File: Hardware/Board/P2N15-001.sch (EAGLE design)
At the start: 36 parts, among them IC1 4053N, IC2 LTC485N, IC3 74LS07N, IC4 LTC485N, X1 HIROSE-DX10LM1-14SE, X2 SUNHAYATO-USB-CK37

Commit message: Redesigned N15 board.
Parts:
- removed IC3: 74LS07N, 74xx-us:74LS07N
- removed IC4: LTC485N, linear-technology:LTC485N
- removed JP3: (no value), pinhead:PINHD-2X3
- removed JP4: (no value), adafruit:PINHD-1X6
- removed LED1, LED2: (no value), led:LED3MM
- removed R10, R11, R12, R7, R8, R9: 220, resistor:R-US_0204/5
- removed R13, R6: 120, resistor:R-US_0204/5
- added S2: TL32PO, switch:TL32PO
- added SV2: (no value), con-ml:ML10L
- IC1: value 4053N -> TLC5941NT; device 40xx:4053N -> adafruit:TLC5941NT
- R3: value 330 -> 4.7k
- R4: value 330 -> 120
- SV1: device con-ml:ML10L -> con-ml:ML20L
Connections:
- removed net ANLG0: JP2.8, MC1.A0, X1.-8
- removed net ANLG1: JP2.9, MC1.A1, X1.-9
- removed net ANLG2: JP2.10, MC1.A2, X1.-10
- removed net ANLG3: JP2.11, MC1.A3, X1.-11
- removed net ANLG4: IC1A.X1, MC1.A4
- removed net ANLG5: IC1A.Y1, MC1.A5
- removed net MISO: JP3.4, MC1.MISO
- removed net RXRETURN: R5.2, SV1.3
- removed net RXSEND: R10.2, SV1.1
- removed net SCL: IC1A.Y0, MC1.3
- removed net SDA: IC1A.X0, MC1.2
- removed net SEL: IC1A.A, IC1A.B, MC1.7
- removed net TX: IC3A.I, IC3B.I, IC4.DI, MC1.TX
- removed net TX+: CN1.1, IC4.A, R13.2
- removed net TX-: CN1.2, IC4.B, R13.1
- removed net TX2RETURN: R11.2, SV1.5
- removed net TX2SEND: R9.2, SV1.4
- removed net TXRETURN: R12.2, SV1.8
- removed net TXSEND: R8.2, SV1.6
- removed net XMIDIRX: IC1A.Z1, IC2.RO
- new net N$10: IC1.OUT3, JP2.10, SV1.6, X1.-10
- new net N$11: IC1.OUT4, JP2.11, SV1.7, X1.-11
- new net N$12: IC1.OUT10, SV1.14
- new net N$13: IC1.OUT11, SV1.13
- new net N$14: IC1.OUT12, SV1.16
- new net N$16: IC1.OUT13, SV1.15
- new net N$7: IC1.OUT1, JP2.8, SV1.4, X1.-8
- new net N$9: IC1.OUT2, JP2.9, SV1.5, X1.-9
- net GND: now also IC1.GND, IC1.MODE, R3.1, SV1.1; no longer IC1A.INH, IC3D.I, IC3E.I, IC3F.I, IC4.GND, JP2.14, JP4.5, R3.2, R4.2, SV1.2, SV1.7, X1.-14
- net GPIO0: now also IC1.GSCLK; no longer JP3.1, LED1.A
- net GPIO1: now also IC1.BLANK; no longer JP3.2, LED2.A
- net GPIO2: now also IC1.XLAT; no longer JP3.3
- net MIDIRX: now also S2.O; no longer IC1A.Z0, IC3C.I
- net MOSI: now also IC1.SIN; no longer JP3.5
- net N$15: now also R5.1; no longer R7.1
- net N$17: now also IC1.OUT14, SV1.18; no longer LED1.C, R3.1
- net N$18: now also IC1.OUT15, SV1.17; no longer LED2.C, R4.1
- net N$2: now also IC2.RO, S2.S; no longer IC3A.O, R11.1
- net N$28: now also IC1.OUT5, SV1.8; no longer IC1A.X
- net N$29: now also IC1.OUT6, SV1.9; no longer IC1A.Y
- net N$3: now also IC1.OUT0, JP2.7, SV1.3, X1.-7; no longer IC3C.O, R5.1
- net N$4: now also IC1.IREF, R3.2; no longer IC3B.O, R12.1
- net N$5: now also IC1.OUT7, JP2.14, SV1.10, X1.-14; no longer JP4.2, MC1.9
- net N$6: now also IC1.OUT8, SV1.12; no longer JP4.3, MC1.10
- net N$8: now also IC1.OUT9, SV1.11; no longer IC1A.C, MC1.4
- net PD: no longer JP4.1
- net RX: now also S2.P
- net RX+: now also R4.2; no longer R6.2
- net RX-: now also R4.1; no longer R6.1
- net RXA: now also R5.2, SV2.9; no longer R7.2, SV1.9
- net RXK: now also SV2.10; no longer SV1.10
- net SCLK: now also IC1.SCLK; no longer JP3.6
- net VCC: now also IC1.TEST, IC1.VCC; no longer IC4.!RE, IC4.DE, IC4.VCC, JP2.7, R10.1, R8.1, R9.1, X1.-7
- net VDD: now also SV1.2
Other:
- note removed: "1: GPIO 0; 2: GPIO 1; 2: GPIO 3; 4: MISO; 5: MOSI; 6: SCLCK"
- note removed: "1: TXA; 2: TXK 3: RXA; 4: RXK"
- moved on the sheet: R3, R4, R5, X2

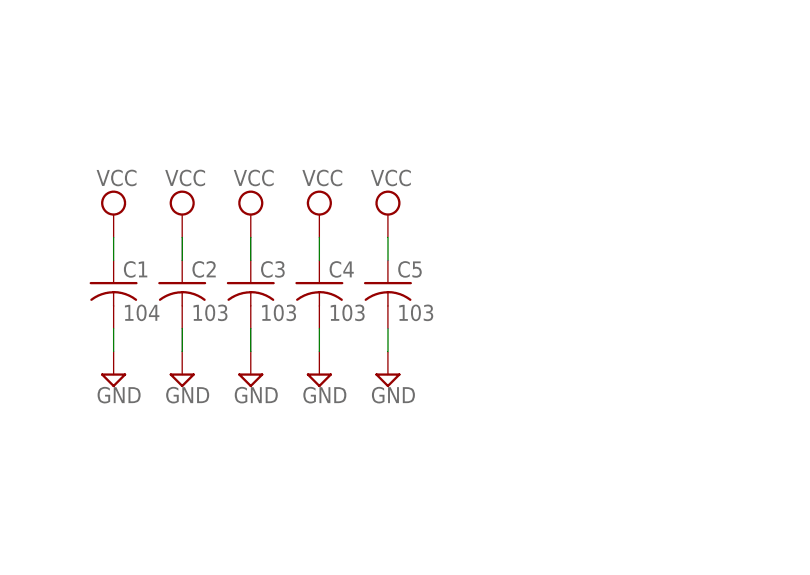
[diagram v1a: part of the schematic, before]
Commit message: Changed 20-p MIL connector type from right-angled to straight.
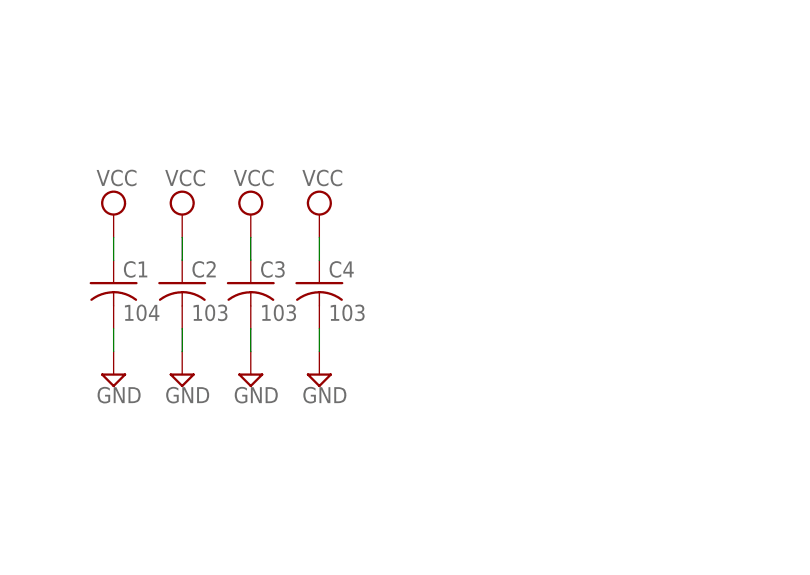
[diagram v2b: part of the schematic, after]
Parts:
- removed C5: 103, rcl:C-US025-025X050
- SV1: device con-ml:ML20L -> con-ml:ML20
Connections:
- net GND: no longer C5.2
- net VCC: no longer C5.1
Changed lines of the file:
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@@
 <part name="C3" library="rcl" deviceset="C-US" device="025-025X050" value="103"/>
 <part name="C4" library="rcl" deviceset="C-US" device="025-025X050" value="103"/>
-<part name="C5" library="rcl" deviceset="C-US" device="025-025X050" value="103"/>
-<part name="SUPPLY24" library="supply2" deviceset="GND" device=""/>
-<part name="SUPPLY23" library="supply2" deviceset="VCC" device=""/>
 <part name="SUPPLY1" library="supply2" deviceset="VCC" device=""/>
 <part name="SUPPLY15" library="supply2" deviceset="VCC" device=""/>
@@
 <part name="SUPPLY4" library="supply2" deviceset="GND" device=""/>
 <part name="SUPPLY2" library="supply2" deviceset="GND" device=""/>
-<part name="SUPPLY25" library="supply2" deviceset="GND" device=""/>
+<part name="SUPPLY23" library="supply2" deviceset="GND" device=""/>
 <part name="VDD1" library="supply1" deviceset="VDD" device=""/>
 <part name="SUPPLY3" library="supply2" deviceset="GND" device=""/>
@@
 <part name="VDD4" library="supply1" deviceset="VDD" device=""/>
 <part name="SUPPLY14" library="supply2" deviceset="GND" device=""/>
-<part name="SV1" library="con-ml" deviceset="ML20L" device=""/>
+<part name="SV1" library="con-ml" deviceset="ML20" device=""/>
 </parts>
 <sheets>
@@
 <instance part="C3" gate="G$1" x="279.4" y="172.72"/>
 <instance part="C4" gate="G$1" x="287.02" y="172.72"/>
-<instance part="C5" gate="G$1" x="294.64" y="172.72"/>
-<instance part="SUPPLY24" gate="GND" x="294.64" y="162.56"/>
-<instance part="SUPPLY23" gate="G$1" x="294.64" y="180.34"/>
 <instance part="SUPPLY1" gate="G$1" x="7.62" y="48.26"/>
 <instance part="SUPPLY15" gate="G$1" x="264.16" y="180.34"/>
@@
 <instance part="SUPPLY4" gate="GND" x="60.96" y="114.3"/>
 <instance part="SUPPLY2" gate="GND" x="40.64" y="114.3"/>
-<instance part="SUPPLY25" gate="GND" x="297.18" y="101.6"/>
+<instance part="SUPPLY23" gate="GND" x="297.18" y="101.6"/>
 <instance part="VDD1" gate="G$1" x="7.62" y="101.6"/>
 <instance part="SUPPLY3" gate="GND" x="40.64" y="83.82"/>
@@
 </segment>
 <segment>
-<pinref part="C5" gate="G$1" pin="2"/>
-<pinref part="SUPPLY24" gate="GND" pin="GND"/>
-<wire x1="294.64" y1="167.64" x2="294.64" y2="165.1" width="0.1524" layer="91"/>
-</segment>
-<segment>
 <pinref part="SUPPLY5" gate="GND" pin="GND"/>
 <wire x1="73.66" y1="25.4" x2="73.66" y2="10.16" width="0.1524" layer="91"/>
@@
 <pinref part="C4" gate="G$1" pin="1"/>
 <wire x1="287.02" y1="177.8" x2="287.02" y2="175.26" width="0.1524" layer="91"/>
-</segment>
-<segment>
-<pinref part="SUPPLY23" gate="G$1" pin="VCC"/>
-<pinref part="C5" gate="G$1" pin="1"/>
-<wire x1="294.64" y1="177.8" x2="294.64" y2="175.26" width="0.1524" layer="91"/>
 </segment>
 <segment>
@@
 </sheet>
 </sheets>
+<errors>
+</errors>
 </schematic>
 </drawing>
